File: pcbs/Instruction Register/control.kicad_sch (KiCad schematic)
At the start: 22 parts, among them U2001 74HC14, U2002 74HC08, U2003 74HC138

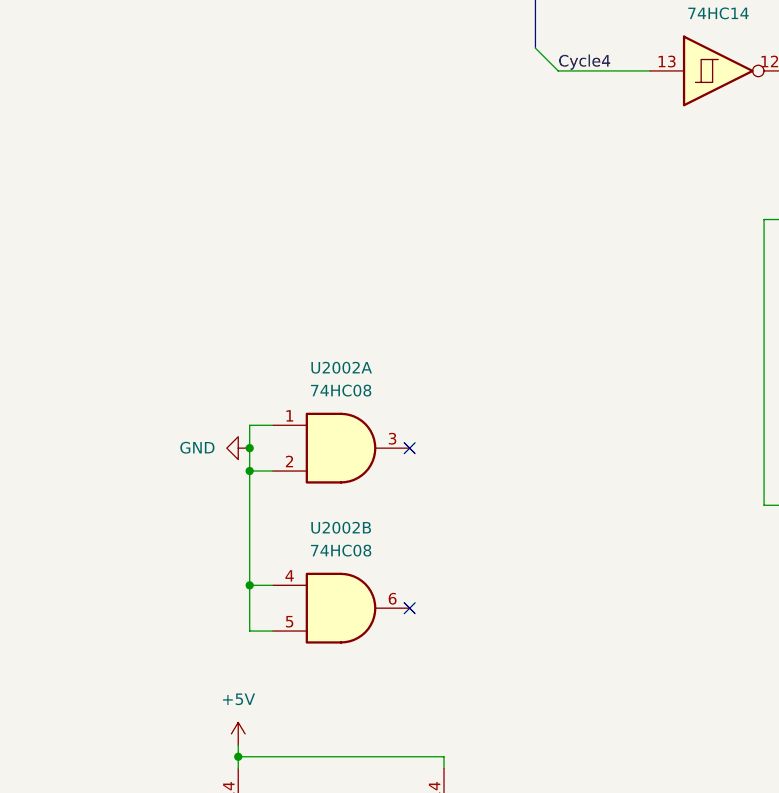
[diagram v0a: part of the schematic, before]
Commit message: Tweaking schematic and basic routing
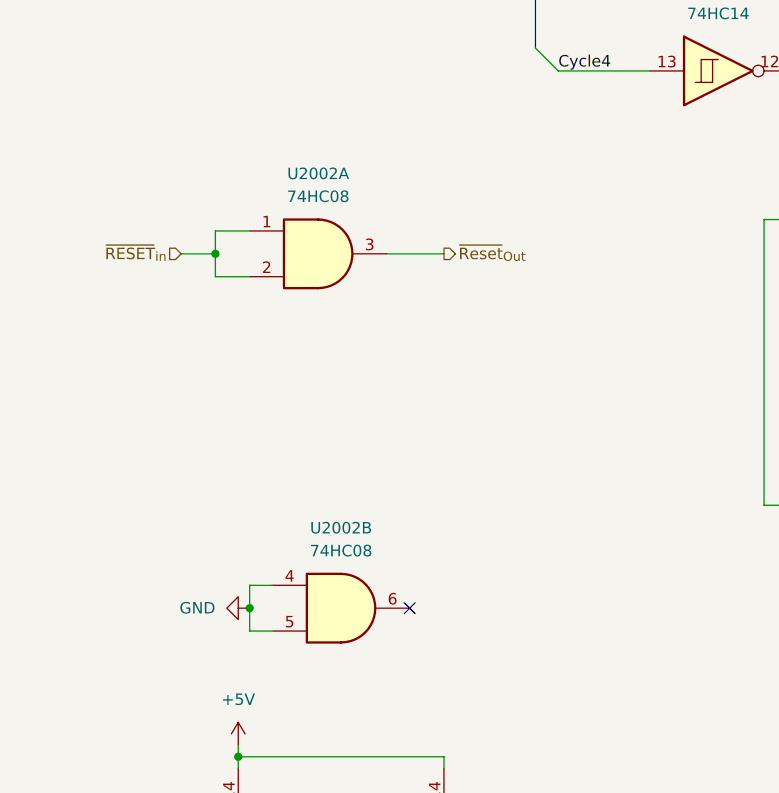
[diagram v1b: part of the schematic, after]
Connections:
- net GND: no longer U2002.1, U2002.2
- net ~{Reset}_{Out}: now reaches U2002.3
- new net ~{RESET}_{in}: U2002.1, U2002.2
- no-connect marks 4 -> 3
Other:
- moved on the sheet: U2002A
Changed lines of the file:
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@@
 	(paper "A3")
-	(junction
-		(at 41.91 189.23)
-		(diameter 0)
-		(color 0 0 0 0)
-	)
-	(junction
-		(at 41.91 191.77)
-		(diameter 0)
-		(color 0 0 0 0)
-	)
 	(junction
 		(at 247.65 129.54)
@@
 	)
 	(junction
-		(at 73.66 91.44)
+		(at 41.91 207.01)
 		(diameter 0)
 		(color 0 0 0 0)
 	)
 	(junction
-		(at 41.91 204.47)
+		(at 38.1 167.64)
+		(diameter 0)
+		(color 0 0 0 0)
+	)
+	(junction
+		(at 73.66 91.44)
 		(diameter 0)
 		(color 0 0 0 0)
@@
 	)
 	(no_connect
-		(at 59.69 189.23)
-	)
-	(no_connect
 		(at 294.64 217.17)
 	)
@@
 	(wire
 		(pts
-			(xy 41.91 204.47) (xy 41.91 191.77)
-		)
-		(stroke
-			(width 0)
-			(type default)
-		)
-	)
-	(wire
-		(pts
 			(xy 139.7 205.74) (xy 139.7 208.28)
 		)
@@
 	(wire
 		(pts
-			(xy 41.91 191.77) (xy 44.45 191.77)
+			(xy 38.1 165.1) (xy 41.91 165.1)
 		)
 		(stroke
@@
 	(wire
 		(pts
-			(xy 41.91 209.55) (xy 41.91 204.47)
+			(xy 41.91 209.55) (xy 41.91 207.01)
 		)
 		(stroke
@@
 	(wire
 		(pts
+			(xy 38.1 167.64) (xy 38.1 165.1)
+		)
+		(stroke
+			(width 0)
+			(type default)
+		)
+	)
+	(wire
+		(pts
 			(xy 40.64 251.46) (xy 63.5 251.46)
 		)
@@
 	(wire
 		(pts
-			(xy 41.91 191.77) (xy 41.91 189.23)
-		)
-		(stroke
-			(width 0)
-			(type default)
-		)
-	)
-	(wire
-		(pts
 			(xy 196.85 125.73) (xy 196.85 129.54)
 		)
@@
 	(wire
 		(pts
+			(xy 34.29 167.64) (xy 38.1 167.64)
+		)
+		(stroke
+			(width 0)
+			(type default)
+		)
+	)
+	(wire
+		(pts
 			(xy 40.64 223.52) (xy 40.64 224.79)
 		)
@@
 		)
 	)
+	(wire
+		(pts
+			(xy 41.91 207.01) (xy 41.91 204.47)
+		)
+		(stroke
+			(width 0)
+			(type default)
+		)
+	)
 	(bus
 		(pts
@@
 	(wire
 		(pts
-			(xy 41.91 189.23) (xy 41.91 186.69)
-		)
-		(stroke
-			(width 0)
-			(type default)
-		)
-	)
-	(wire
-		(pts
 			(xy 209.55 105.41) (xy 209.55 107.95)
 		)
@@
 	(wire
 		(pts
-			(xy 41.91 186.69) (xy 44.45 186.69)
-		)
-		(stroke
-			(width 0)
-			(type default)
-		)
-	)
-	(wire
-		(pts
 			(xy 76.2 147.32) (xy 86.36 147.32)
 		)
@@
 	(wire
 		(pts
+			(xy 38.1 167.64) (xy 38.1 170.18)
+		)
+		(stroke
+			(width 0)
+			(type default)
+		)
+	)
+	(wire
+		(pts
 			(xy 182.88 242.57) (xy 182.88 246.38)
 		)
@@
 		(pts
 			(xy 99.06 195.58) (xy 129.54 195.58)
+		)
+		(stroke
+			(width 0)
+			(type default)
+		)
+	)
+	(wire
+		(pts
+			(xy 38.1 170.18) (xy 41.91 170.18)
+		)
+		(stroke
+			(width 0)
+			(type default)
+		)
+	)
+	(wire
+		(pts
+			(xy 57.15 167.64) (xy 63.5 167.64)
 		)
 		(stroke
@@
 		)
 	)
+	(hierarchical_label "~{Reset}_{Out}"
+		(shape output)
+		(at 63.5 167.64 0)
+		(fields_autoplaced yes)
+		(effects
+			(font
+				(size 1.27 1.27)
+			)
+			(justify left)
+		)
+	)
 	(hierarchical_label "~{Set}"
 		(shape output)
@@
 			)
 			(justify left)
+		)
+	)
+	(hierarchical_label "~{RESET}_{in}"
+		(shape input)
+		(at 34.29 167.64 180)
+		(fields_autoplaced yes)
+		(effects
+			(font
+				(size 1.27 1.27)
+			)
+			(justify right)
 		)
 	)
@@
 	(symbol
 		(lib_id "74xx:74LS08")
-		(at 52.07 189.23 0)
+		(at 49.53 167.64 0)
 		(unit 1)
 		(exclude_from_sim no)
@@
 		(fields_autoplaced yes)
 		(property "Reference" "U2002"
-			(at 52.0617 180.34 0)
+			(at 49.5217 158.75 0)
 			(effects
 				(font
@@
 		)
 		(property "Value" "74HC08"
-			(at 52.0617 182.88 0)
+			(at 49.5217 161.29 0)
 			(effects
 				(font
@@
 		)
 		(property "Footprint" "Package_SO:SOIC-14_3.9x8.7mm_P1.27mm"
-			(at 52.07 189.23 0)
+			(at 49.53 167.64 0)
 			(effects
 				(font
@@
 		)
 		(property "Datasheet" "https://www.lcsc.com/datasheet/lcsc_datasheet_2407241044_Nexperia-74HC08D-653_C5593.pdf"
-			(at 52.07 189.23 0)
+			(at 49.53 167.64 0)
 			(effects
 				(font
@@
 		)
 		(property "Description" "Quad And2"
-			(at 52.07 189.23 0)
+			(at 49.53 167.64 0)
 			(effects
 				(font
@@
 		)
 		(property "LCSC" "C5593"
-			(at 52.07 189.23 0)
+			(at 49.53 167.64 0)
 			(effects
 				(font
@@
 	(symbol
 		(lib_id "power:GND")
-		(at 41.91 189.23 270)
+		(at 41.91 207.01 270)
 		(unit 1)
 		(exclude_from_sim no)
@@
 		(fields_autoplaced yes)
 		(property "Reference" "#PWR02003"
-			(at 35.56 189.23 0)
+			(at 35.56 207.01 0)
 			(effects
 				(font
@@
 		)
 		(property "Value" "GND"
-			(at 38.1 189.2299 90)
+			(at 38.1 207.0099 90)
 			(effects
 				(font
@@
 		)
 		(property "Footprint" ""
-			(at 41.91 189.23 0)
+			(at 41.91 207.01 0)
 			(effects
 				(font
@@
 		)
 		(property "Datasheet" ""
-			(at 41.91 189.23 0)
+			(at 41.91 207.01 0)
 			(effects
 				(font
@@
 		)
 		(property "Description" "Power symbol creates a global label with name \"GND\" , ground"
-			(at 41.91 189.23 0)
-			(effects
-				(font
+			(at 41.91 207.01 0)
+			(effects
+				(font
